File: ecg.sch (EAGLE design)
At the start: 21 parts, among them IC1 ADP151, U1 TMP102AIDRLT, U2 TMP102AIDRLT, U3 ADAS1000BSTZ

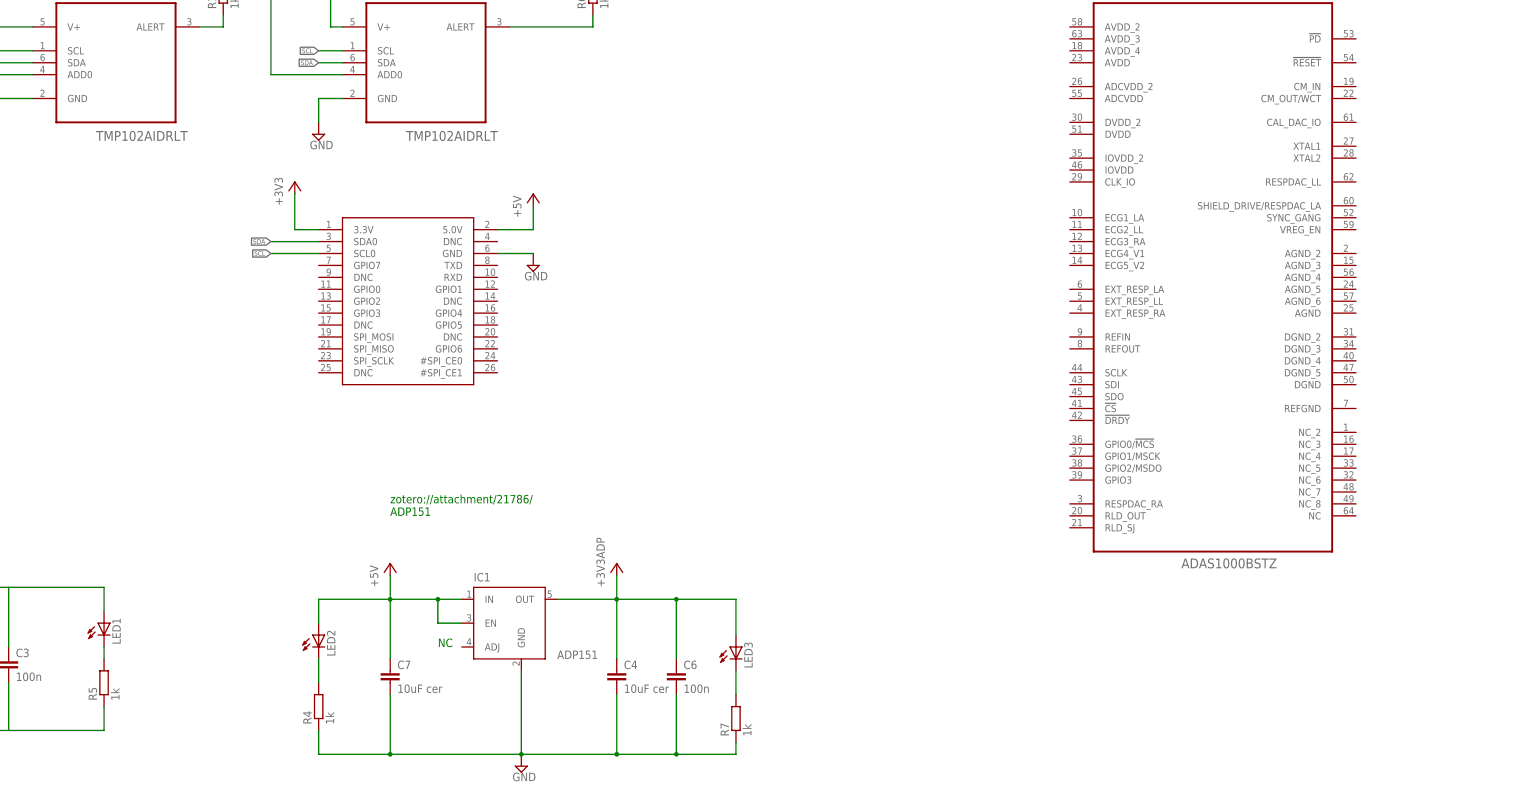
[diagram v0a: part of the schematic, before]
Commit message: Added XTAL
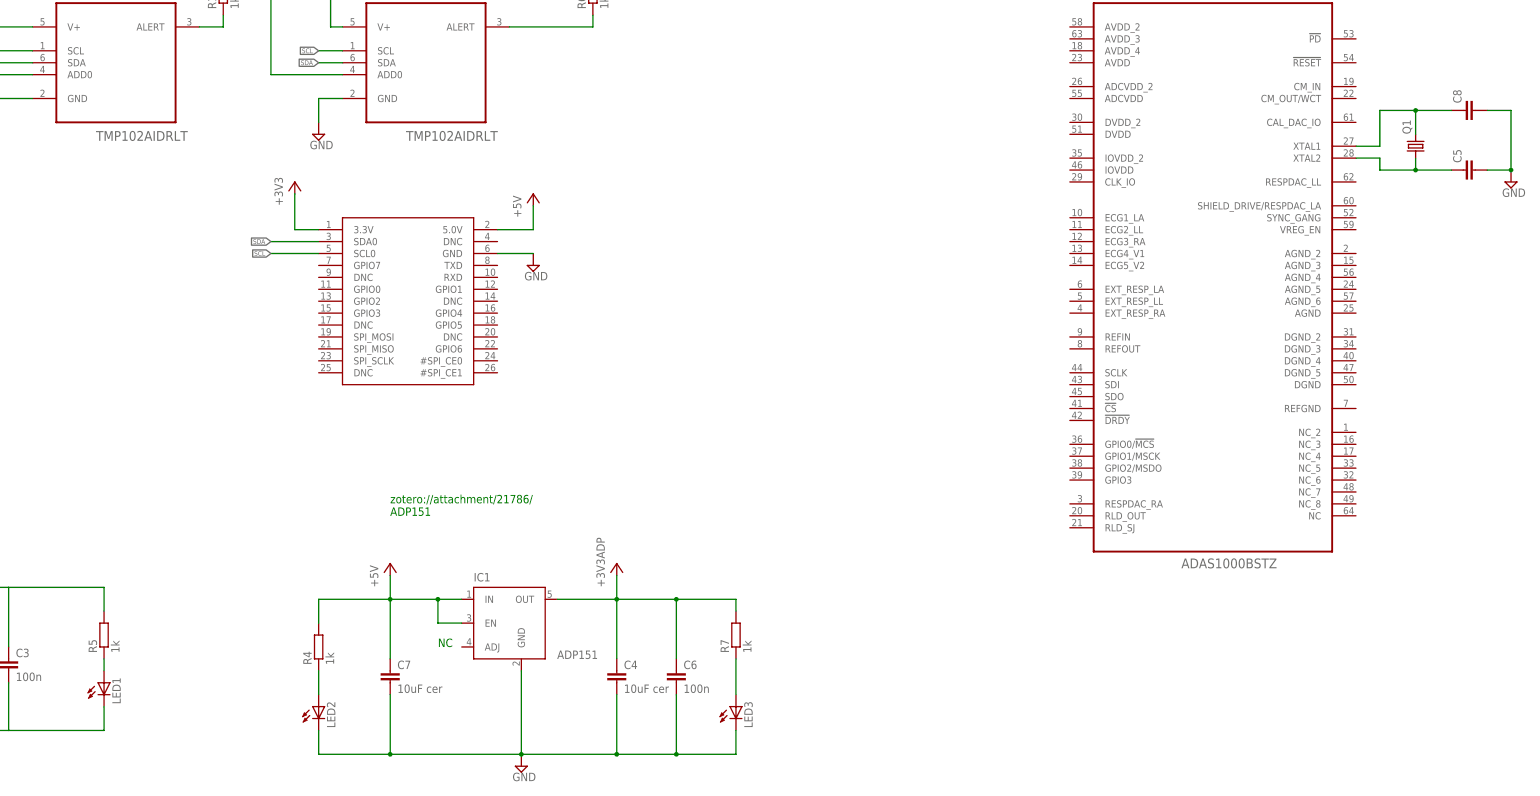
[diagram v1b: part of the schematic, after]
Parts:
- added C5, C8: (no value), rcl:C-EUC0201
- added Q1: (no value), crystal:CRYSTALHC49UP
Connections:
- new net N$3: LED2.A, R4.1
- new net N$6: C5.1, Q1.1, U3.XTAL2
- net +3V3: now also R5.2, R7.2; no longer LED1.A, LED3.A
- net +5V: now also R4.2; no longer LED2.A
- net GND: now also C5.2, C8.2, LED1.C, LED2.C, LED3.C; no longer R4.1, R5.1, R7.1
- net N$2: now also LED1.A, R5.1; no longer LED1.C, R5.2
- net N$5: now also LED3.A, R7.1; no longer LED2.C, R4.2
- net N$7: now also C8.1, Q1.2, U3.XTAL1; no longer LED3.C, R7.2
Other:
- moved on the sheet: LED1, LED2, LED3, R4, R5, R7
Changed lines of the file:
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@@
 <part name="C7" library="resistor" deviceset="C-EU" device="C0805K" value="10uF cer"/>
 <part name="C4" library="resistor" deviceset="C-EU" device="C0805K" value="10uF cer"/>
+<part name="Q1" library="crystal" deviceset="CRYSTAL" device="HC49UP"/>
+<part name="C5" library="rcl" deviceset="C-EU" device="C0201"/>
+<part name="C8" library="rcl" deviceset="C-EU" device="C0201"/>
+<part name="SUPPLY6" library="supply2" deviceset="GND" device=""/>
 </parts>
 <sheets>
@@
 <instance part="+3V2" gate="G$1" x="106.68" y="134.62"/>
 <instance part="SUPPLY4" gate="GND" x="111.76" y="144.78"/>
-<instance part="LED1" gate="G$1" x="66.04" y="40.64"/>
-<instance part="R5" gate="G$1" x="66.04" y="27.94" rot="R90"/>
+<instance part="LED1" gate="G$1" x="66.04" y="27.94"/>
+<instance part="R5" gate="G$1" x="66.04" y="38.1" rot="R90"/>
 <instance part="+3V3" gate="G$1" x="30.48" y="60.96"/>
 <instance part="P+1" gate="1" x="127" y="53.34"/>
@@
 <instance part="+3V4" gate="G$1" x="175.26" y="53.34"/>
 <instance part="C6" gate="G$1" x="187.96" y="30.48"/>
-<instance part="LED2" gate="G$1" x="111.76" y="38.1"/>
-<instance part="R4" gate="G$1" x="111.76" y="22.86" rot="R90"/>
-<instance part="LED3" gate="G$1" x="200.66" y="35.56"/>
-<instance part="R7" gate="G$1" x="200.66" y="20.32" rot="R90"/>
+<instance part="LED2" gate="G$1" x="111.76" y="22.86"/>
+<instance part="R4" gate="G$1" x="111.76" y="35.56" rot="R90"/>
+<instance part="LED3" gate="G$1" x="200.66" y="22.86"/>
+<instance part="R7" gate="G$1" x="200.66" y="38.1" rot="R90"/>
 <instance part="C7" gate="G$1" x="127" y="30.48"/>
 <instance part="C4" gate="G$1" x="175.26" y="30.48"/>
+<instance part="Q1" gate="G$1" x="345.44" y="142.24" rot="R90"/>
+<instance part="C5" gate="G$1" x="355.6" y="137.16" rot="R90"/>
+<instance part="C8" gate="G$1" x="355.6" y="149.86" rot="R90"/>
+<instance part="SUPPLY6" gate="GND" x="365.76" y="134.62"/>
 </instances>
 <busses>
@@
 <wire x1="45.72" y1="27.94" x2="45.72" y2="17.78" width="0.1524" layer="91"/>
 <wire x1="45.72" y1="17.78" x2="30.48" y2="17.78" width="0.1524" layer="91"/>
-<pinref part="R5" gate="G$1" pin="1"/>
 <wire x1="45.72" y1="17.78" x2="66.04" y2="17.78" width="0.1524" layer="91"/>
-<wire x1="66.04" y1="17.78" x2="66.04" y2="22.86" width="0.1524" layer="91"/>
+<pinref part="LED1" gate="G$1" pin="C"/>
+<wire x1="66.04" y1="22.86" x2="66.04" y2="17.78" width="0.1524" layer="91"/>
 </segment>
 <segment>
@@
 <pinref part="C6" gate="G$1" pin="2"/>
 <wire x1="187.96" y1="25.4" x2="187.96" y2="12.7" width="0.1524" layer="91"/>
-<pinref part="R4" gate="G$1" pin="1"/>
-<wire x1="111.76" y1="17.78" x2="111.76" y2="12.7" width="0.1524" layer="91"/>
 <wire x1="111.76" y1="12.7" x2="127" y2="12.7" width="0.1524" layer="91"/>
 <junction x="127" y="12.7"/>
-<pinref part="R7" gate="G$1" pin="1"/>
-<wire x1="200.66" y1="15.24" x2="200.66" y2="12.7" width="0.1524" layer="91"/>
 <wire x1="200.66" y1="12.7" x2="187.96" y2="12.7" width="0.1524" layer="91"/>
 <junction x="187.96" y="12.7"/>
@@
 <wire x1="175.26" y1="25.4" x2="175.26" y2="12.7" width="0.1524" layer="91"/>
 <junction x="175.26" y="12.7"/>
+<pinref part="LED2" gate="G$1" pin="C"/>
+<wire x1="111.76" y1="17.78" x2="111.76" y2="12.7" width="0.1524" layer="91"/>
+<pinref part="LED3" gate="G$1" pin="C"/>
+<wire x1="200.66" y1="12.7" x2="200.66" y2="17.78" width="0.1524" layer="91"/>
+</segment>
+<segment>
+<pinref part="C8" gate="G$1" pin="2"/>
+<pinref part="SUPPLY6" gate="GND" pin="GND"/>
+<wire x1="360.68" y1="149.86" x2="365.76" y2="149.86" width="0.1524" layer="91"/>
+<wire x1="365.76" y1="149.86" x2="365.76" y2="137.16" width="0.1524" layer="91"/>
+<pinref part="C5" gate="G$1" pin="2"/>
+<wire x1="365.76" y1="137.16" x2="360.68" y2="137.16" width="0.1524" layer="91"/>
+<junction x="365.76" y="137.16"/>
 </segment>
 </net>
@@
 <pinref part="+3V3" gate="G$1" pin="+3V3"/>
 <wire x1="30.48" y1="58.42" x2="30.48" y2="48.26" width="0.1524" layer="91"/>
-<pinref part="LED1" gate="G$1" pin="A"/>
 <wire x1="45.72" y1="48.26" x2="66.04" y2="48.26" width="0.1524" layer="91"/>
+<pinref part="R5" gate="G$1" pin="2"/>
 <wire x1="66.04" y1="48.26" x2="66.04" y2="43.18" width="0.1524" layer="91"/>
 </segment>
@@
 <wire x1="187.96" y1="45.72" x2="187.96" y2="33.02" width="0.1524" layer="91"/>
 <junction x="175.26" y="45.72"/>
-<pinref part="LED3" gate="G$1" pin="A"/>
 <wire x1="187.96" y1="45.72" x2="200.66" y2="45.72" width="0.1524" layer="91"/>
-<wire x1="200.66" y1="45.72" x2="200.66" y2="38.1" width="0.1524" layer="91"/>
 <junction x="187.96" y="45.72"/>
 <pinref part="C4" gate="G$1" pin="1"/>
-</segment>
-</net>
-<net name="N$2" class="0">
-<segment>
-<pinref part="R5" gate="G$1" pin="2"/>
-<pinref part="LED1" gate="G$1" pin="C"/>
-<wire x1="66.04" y1="33.02" x2="66.04" y2="35.56" width="0.1524" layer="91"/>
+<pinref part="R7" gate="G$1" pin="2"/>
+<wire x1="200.66" y1="45.72" x2="200.66" y2="43.18" width="0.1524" layer="91"/>
 </segment>
 </net>
@@
 <pinref part="IC1" gate="G1" pin="IN"/>
 <junction x="137.16" y="45.72"/>
-<pinref part="LED2" gate="G$1" pin="A"/>
-<wire x1="111.76" y1="40.64" x2="111.76" y2="45.72" width="0.1524" layer="91"/>
 <wire x1="111.76" y1="45.72" x2="127" y2="45.72" width="0.1524" layer="91"/>
 <pinref part="C7" gate="G$1" pin="1"/>
 <wire x1="127" y1="33.02" x2="127" y2="45.72" width="0.1524" layer="91"/>
+<pinref part="R4" gate="G$1" pin="2"/>
+<wire x1="111.76" y1="40.64" x2="111.76" y2="45.72" width="0.1524" layer="91"/>
+</segment>
+</net>
+<net name="N$2" class="0">
+<segment>
+<pinref part="R5" gate="G$1" pin="1"/>
+<pinref part="LED1" gate="G$1" pin="A"/>
+<wire x1="66.04" y1="33.02" x2="66.04" y2="30.48" width="0.1524" layer="91"/>
+</segment>
+</net>
+<net name="N$3" class="0">
+<segment>
+<pinref part="R4" gate="G$1" pin="1"/>
+<pinref part="LED2" gate="G$1" pin="A"/>
+<wire x1="111.76" y1="30.48" x2="111.76" y2="25.4" width="0.1524" layer="91"/>
 </segment>
 </net>
 <net name="N$5" class="0">
 <segment>
-<pinref part="LED2" gate="G$1" pin="C"/>
-<pinref part="R4" gate="G$1" pin="2"/>
-<wire x1="111.76" y1="33.02" x2="111.76" y2="27.94" width="0.1524" layer="91"/>
+<pinref part="R7" gate="G$1" pin="1"/>
+<pinref part="LED3" gate="G$1" pin="A"/>
+<wire x1="200.66" y1="33.02" x2="200.66" y2="25.4" width="0.1524" layer="91"/>
 </segment>
 </net>
 <net name="N$7" class="0">
 <segment>
-<pinref part="LED3" gate="G$1" pin="C"/>
-<pinref part="R7" gate="G$1" pin="2"/>
-<wire x1="200.66" y1="30.48" x2="200.66" y2="25.4" width="0.1524" layer="91"/>
-</segment>
-</net>
+<pinref part="U3" gate="A" pin="XTAL1"/>
+<wire x1="332.74" y1="142.24" x2="337.82" y2="142.24" width="0.1524" layer="91"/>
+<wire x1="337.82" y1="142.24" x2="337.82" y2="149.86" width="0.1524" layer="91"/>
+<pinref part="Q1" gate="G$1" pin="2"/>
+<wire x1="337.82" y1="149.86" x2="345.44" y2="149.86" width="0.1524" layer="91"/>
+<wire x1="345.44" y1="149.86" x2="345.44" y2="144.78" width="0.1524" layer="91"/>
+<pinref part="C8" gate="G$1" pin="1"/>
+<wire x1="345.44" y1="149.86" x2="353.06" y2="149.86" width="0.1524" layer="91"/>
+<junction x="345.44" y="149.86"/>
+</segment>
+</net>
+<net name="N$6" class="0">
+<segment>
+<pinref part="U3" gate="A" pin="XTAL2"/>
+<wire x1="332.74" y1="139.7" x2="337.82" y2="139.7" width="0.1524" layer="91"/>
+<wire x1="337.82" y1="139.7" x2="337.82" y2="137.16" width="0.1524" layer="91"/>
+<wire x1="337.82" y1="137.16" x2="345.44" y2="137.16" width="0.1524" layer="91"/>
+<pinref part="Q1" gate="G$1" pin="1"/>
+<wire x1="345.44" y1="137.16" x2="345.44" y2="139.7" width="0.1524" layer="91"/>
+<pinref part="C5" gate="G$1" pin="1"/>
+<wire x1="345.44" y1="137.16" x2="353.06" y2="137.16" width="0.1524" layer="91"/>
+<junction x="345.44" y="137.16"/>
+</segment>
+</net>

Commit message: Added second voltage regulator for digital domain. Changed the frame to a bigger one.
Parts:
- added C10, C11: 10uF cer, resistor:C-EUC0805K
- added C9: 100n, eagle-ltspice:CC0603
- added IC2: ADP151, v-reg-micrel:MIC5219BM5
- added LED4, LED5: (no value), eagle-ltspice:LED_ESML0603
- added R10, R9: 1k, resistor:R-EU_R0603
- added R11, R8: 10k, resistor:R-EU_R0603
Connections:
- new net +3V3ADCVDD: C4.1, C6.1, IC1.OUT, R7.2
- new net +3V3IOVDD: C11.1, C9.1, IC2.OUT, R10.2
- new net N$10: LED5.A, R10.1
- new net N$11: IC2.EN, R11.1
- new net N$8: IC1.EN, R8.1
- new net N$9: LED4.A, R9.1
- net +3V3: no longer C4.1, C6.1, IC1.OUT, R7.2
- net +5V: now also C10.1, IC2.IN, R11.2, R8.2, R9.2; no longer IC1.EN
- net GND: now also C10.2, C11.2, C9.2, IC2.GND, LED4.C, LED5.C
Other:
- moved on the sheet: C5, C8, Q1, U3
